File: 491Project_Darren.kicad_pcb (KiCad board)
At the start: 4 copper layers, 77 x 77 mm, 49 parts, among them J1 RJ45, J2 RJ45, J3 Conn_01x10_MountingPin

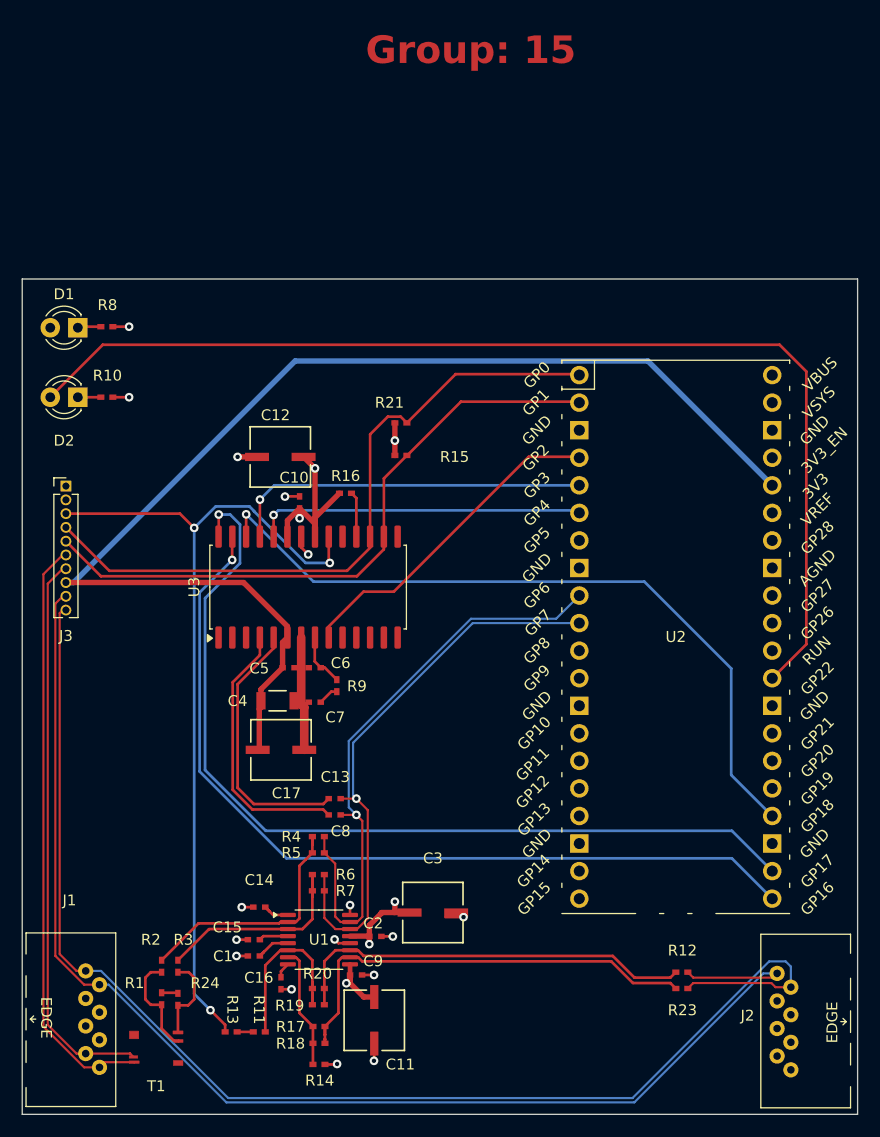
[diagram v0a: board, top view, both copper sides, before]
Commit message: changes 0402 footprints to 0805
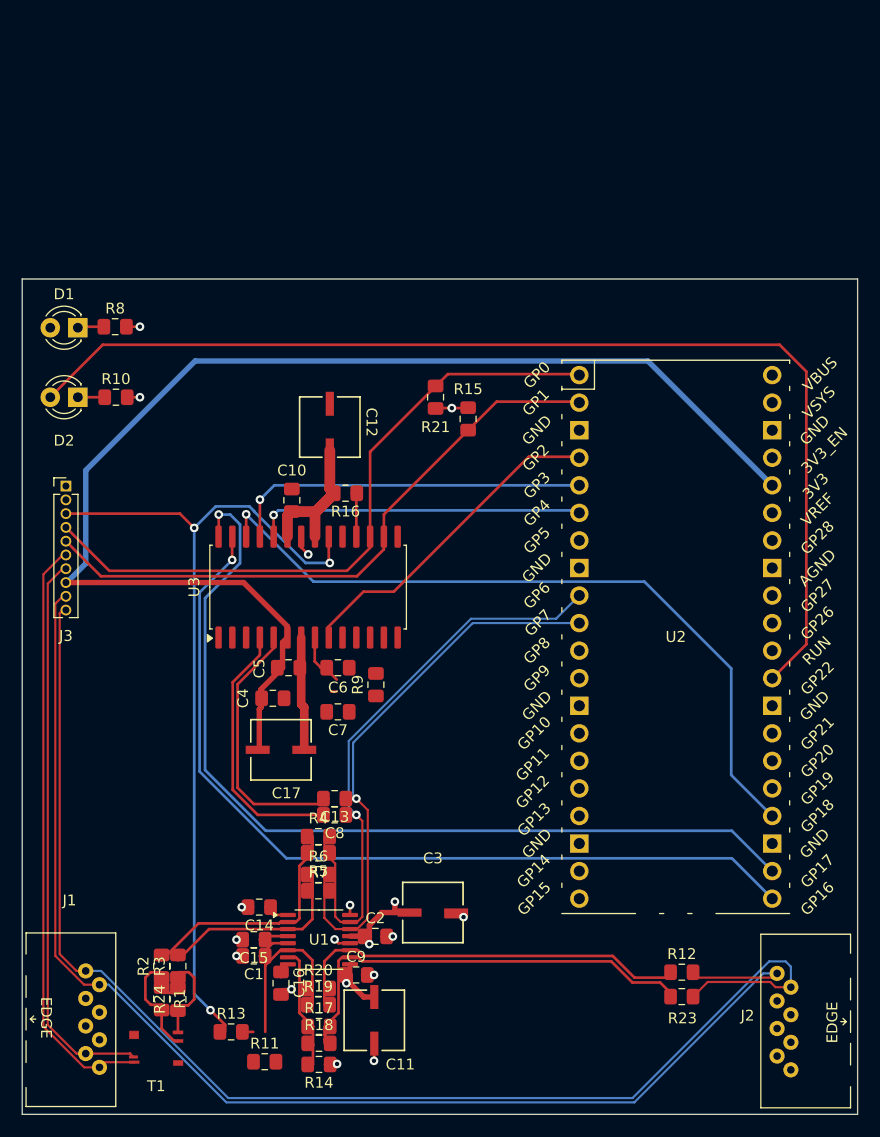
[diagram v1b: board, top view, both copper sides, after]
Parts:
- C1, C10, C13, C14, C15, C16, C2, C5, C6, C7, C8, C9: footprint 491_Footprints:CAP_805_CER -> Capacitor_SMD:C_0805_2012Metric_Pad1.18x1.45mm_HandSolder
- C4: footprint 491_Footprints:CAP_CER_0.1uF_1206 -> Capacitor_SMD:C_0805_2012Metric_Pad1.18x1.45mm_HandSolder
- R1, R10, R12, R14, R15, R16, R17, R18, R19, R2, R20, R21, R23, R24, R3, R4, R5, R6, R7, R8, R9: footprint 491_Footprints:R_805 -> Capacitor_SMD:C_0805_2012Metric_Pad1.18x1.45mm_HandSolder
- R11: value 100 -> 0; footprint 491_Footprints:R_805 -> Capacitor_SMD:C_0805_2012Metric_Pad1.18x1.45mm_HandSolder
- R13: value 900 -> 1k; footprint 491_Footprints:R_805 -> Capacitor_SMD:C_0805_2012Metric_Pad1.18x1.45mm_HandSolder
- moved R15 7.05 mm to (148.2, 76.0), turned to 90 degrees
- moved C12 5.33 mm to (135.5, 76.8), turned to 90 degrees
- moved R21 3.98 mm to (145.2, 74.0), turned to -90 degrees
- moved R9 3.61 mm to (139.8, 100.5)
- moved R11 2.80 mm to (129.5, 135.2)
- moved C7 2.32 mm to (136.2, 103.0)
- moved C6 2.14 mm to (136.2, 98.9)
- moved R10 0.84 mm to (115.8, 74.0)
- moved R8 0.77 mm to (115.7, 67.5)
- moved R23 0.75 mm to (167.9, 129.2)
- moved C10 0.74 mm to (132.0, 83.5)
- moved C4 0.49 mm to (130.2, 101.8)
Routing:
- net VA: track 112.9 -> 117.9 mm
- net +5V: track 37.7 -> 33.5 mm, vias 6 -> 4
- net GND: track 21.2 -> 17.5 mm, vias 16 -> 14
- net SCL: track 59.2 -> 57.2 mm
- net Net-(C7-Pad1): track 1.88 -> 0.00 mm
- net SDA: track 63.1 -> 61.7 mm
- net GNDA: track 10.5 -> 11.0 mm
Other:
- board text added: "Group: 14"
- board text removed: "Group: 15"
- board text removed: "Group: XX"

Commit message: updated silkscreen text to 40 mils
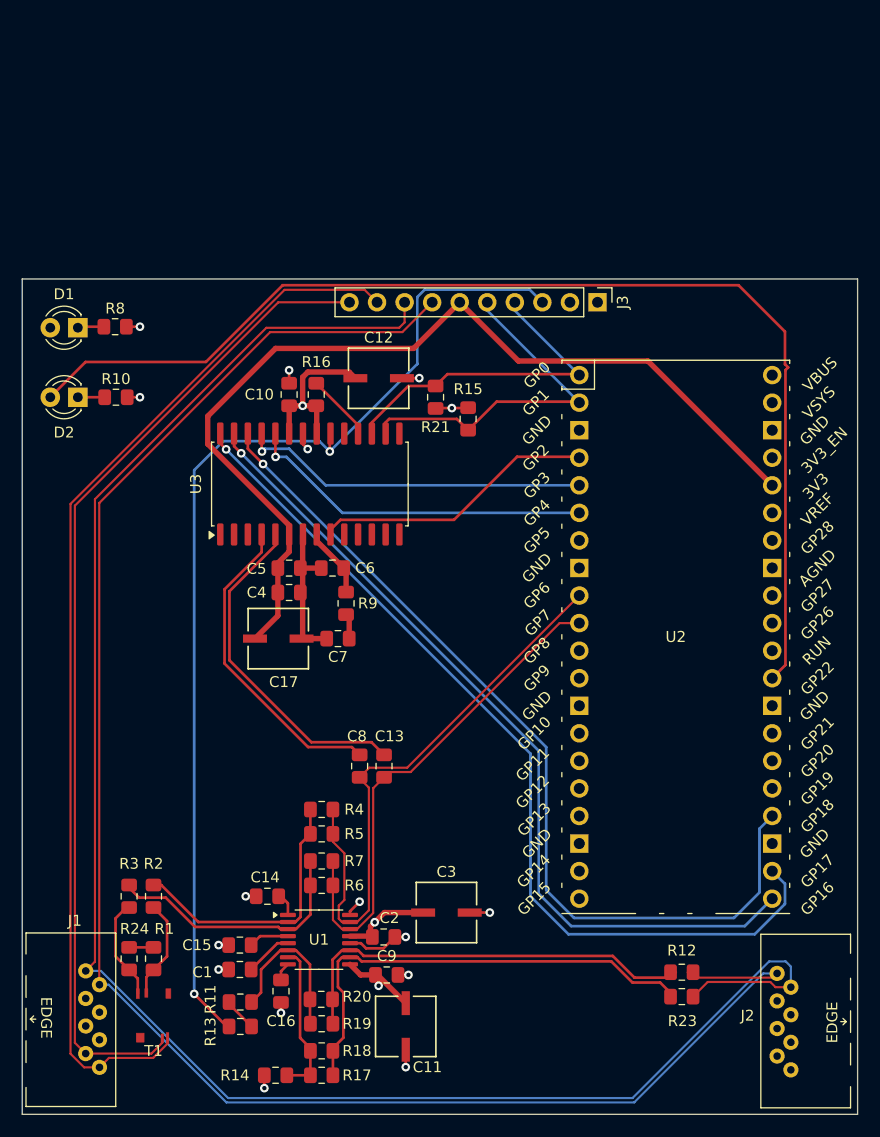
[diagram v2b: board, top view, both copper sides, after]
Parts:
- J3: footprint Connector_PinHeader_1.27mm:PinHeader_1x10_P1.27mm_Vertical -> Connector_PinHeader_2.54mm:PinHeader_1x10_P2.54mm_Vertical
- moved J3 51.8 mm to (160.2, 65.2), turned to -90 degrees
- moved C17 10.3 mm to (130.8, 96.2)
- moved C4 9.86 mm to (131.8, 92.0)
- moved C10 9.75 mm to (131.8, 73.8)
- moved U3 9.50 mm to (133.7, 82.0)
- moved R16 9.49 mm to (134.2, 73.8), turned to -90 degrees
- moved C6 9.20 mm to (135.8, 89.8)
- moved C5 9.18 mm to (131.8, 89.8)
- moved R9 7.99 mm to (137.0, 93.0)
- moved R3 7.86 mm to (117.0, 120.0)
- moved C7 6.75 mm to (136.2, 96.2)
- moved R2 6.49 mm to (119.2, 120.0)
- moved C12 6.36 mm to (140.0, 72.2), turned to 0 degrees
- moved R11 5.94 mm to (127.2, 129.8)
- moved R24 5.86 mm to (117.0, 125.8)
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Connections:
- J3 pad 10: SIG_OUT+ -> SIG_IN+
- J3 pad 6: SIG_IN- -> VA
- J3 pad 7: SIG_IN+ -> SIG_OUT-
- J3 pad 8: VA -> SIG_OUT+
- J3 pad 9: SIG_OUT- -> SIG_IN-
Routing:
- net SIG_OUT+: track 122.0 -> 167.9 mm
- net SIG_IN-: track 54.5 -> 98.5 mm
- net SIG_OUT-: track 119.4 -> 163.4 mm
- net SIG_IN+: track 51.9 -> 91.9 mm
- net SDA: track 61.7 -> 31.2 mm
- net VA: track 117.9 -> 88.3 mm
- net SCL: track 57.2 -> 33.3 mm
- net PASS+: track 78.0 -> 98.3 mm, vias 3 -> 2
- net SDOUT: track 67.8 -> 82.7 mm
- net Net-(U3-RXN): track 24.5 -> 31.2 mm
- net GND: track 17.5 -> 23.8 mm, vias 14 -> 15
- net AES3-: track 52.5 -> 46.9 mm, vias 1 -> 0
- net RST: track 30.6 -> 26.2 mm
- net Net-(U3-RXP0): track 24.9 -> 29.2 mm
- net LED: track 102.2 -> 106.4 mm
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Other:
- board text removed: "Design Guidelines: Do not change the board outline on the edge.cuts layer. Update the group identifier on both the copper layer and paste mask, otherwise you may get the wrong stencil. No components on the backside of the board unless you design them to be hand soldered, no smaller than 0805, use of 0603 will have to be cleared with either Jordan (jmh25@sfu.ca) or Patrick (ppalmer@sfu.ca) (have a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"
- board text removed: "Group: 14"
- board text removed: "Tips & Tricks To bulk change object properties go to Edit -> {dblquote}Edit ___ & ___ properties{dblquote}"
